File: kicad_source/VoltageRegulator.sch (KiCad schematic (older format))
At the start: 45 parts, among them CN6 691313710002, Q1 IPD90P03P4L- 04, U3 LM1085ISX-ADJ/NOPB, U9 IFX91041EJV

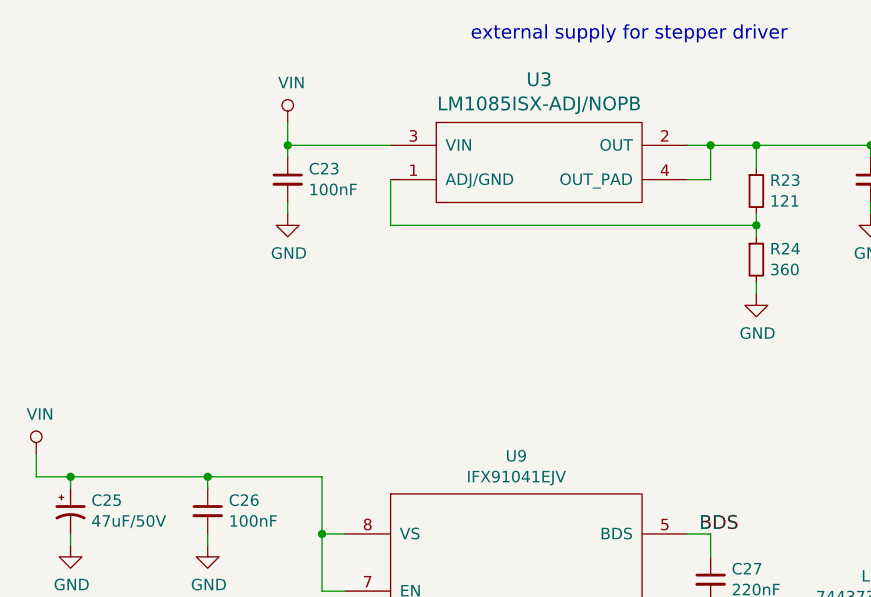
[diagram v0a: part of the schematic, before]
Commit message: corrected position of mounting holes for heat spreader, added information on input voltage
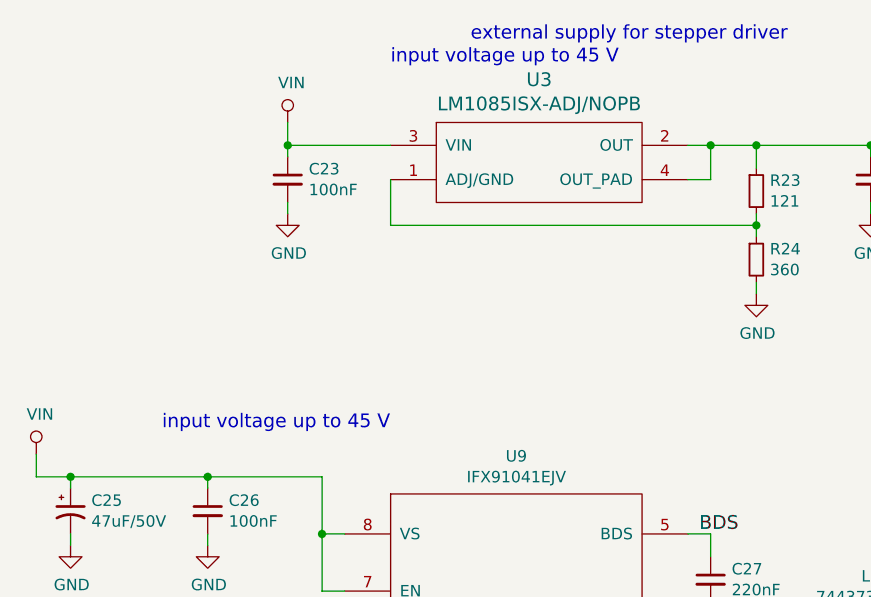
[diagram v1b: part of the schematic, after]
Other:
- note added: "input voltage up to 45 V"
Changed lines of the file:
@@
 Text Notes 4950 1200 0    60   ~ 0
 external supply for stepper driver
+Text Notes 3600 2900 0    60   ~ 0
+input voltage up to 45 V
+Text Notes 4600 1300 0    60   ~ 0
+input voltage up to 45 V
 $EndSCHEMATC

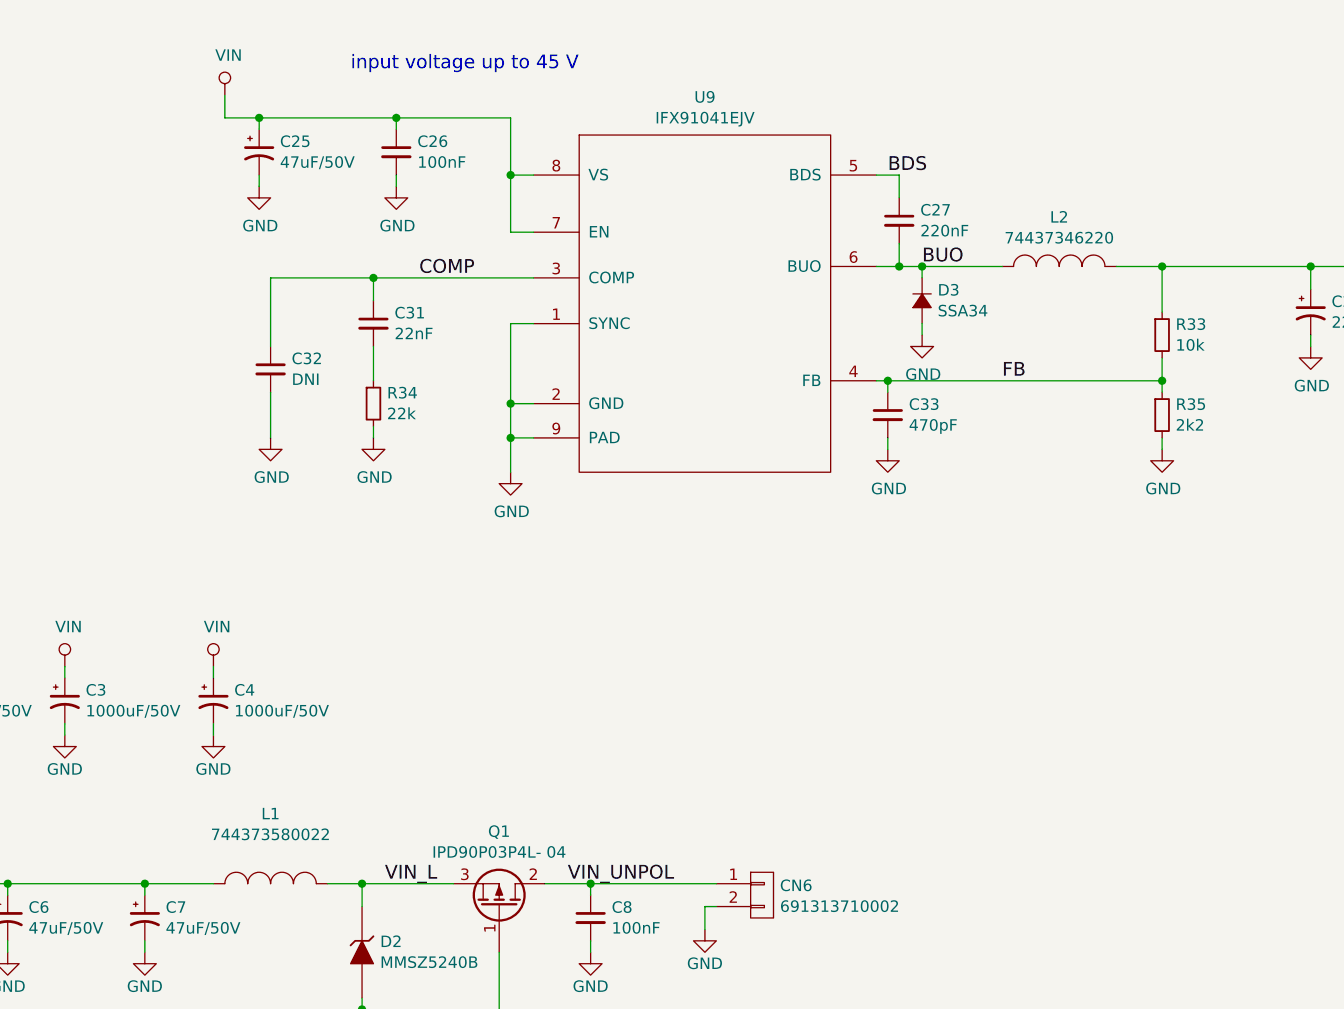
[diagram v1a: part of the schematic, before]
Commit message: changed L1 and L2 to Sumida 0624CDMCCDS for better availability
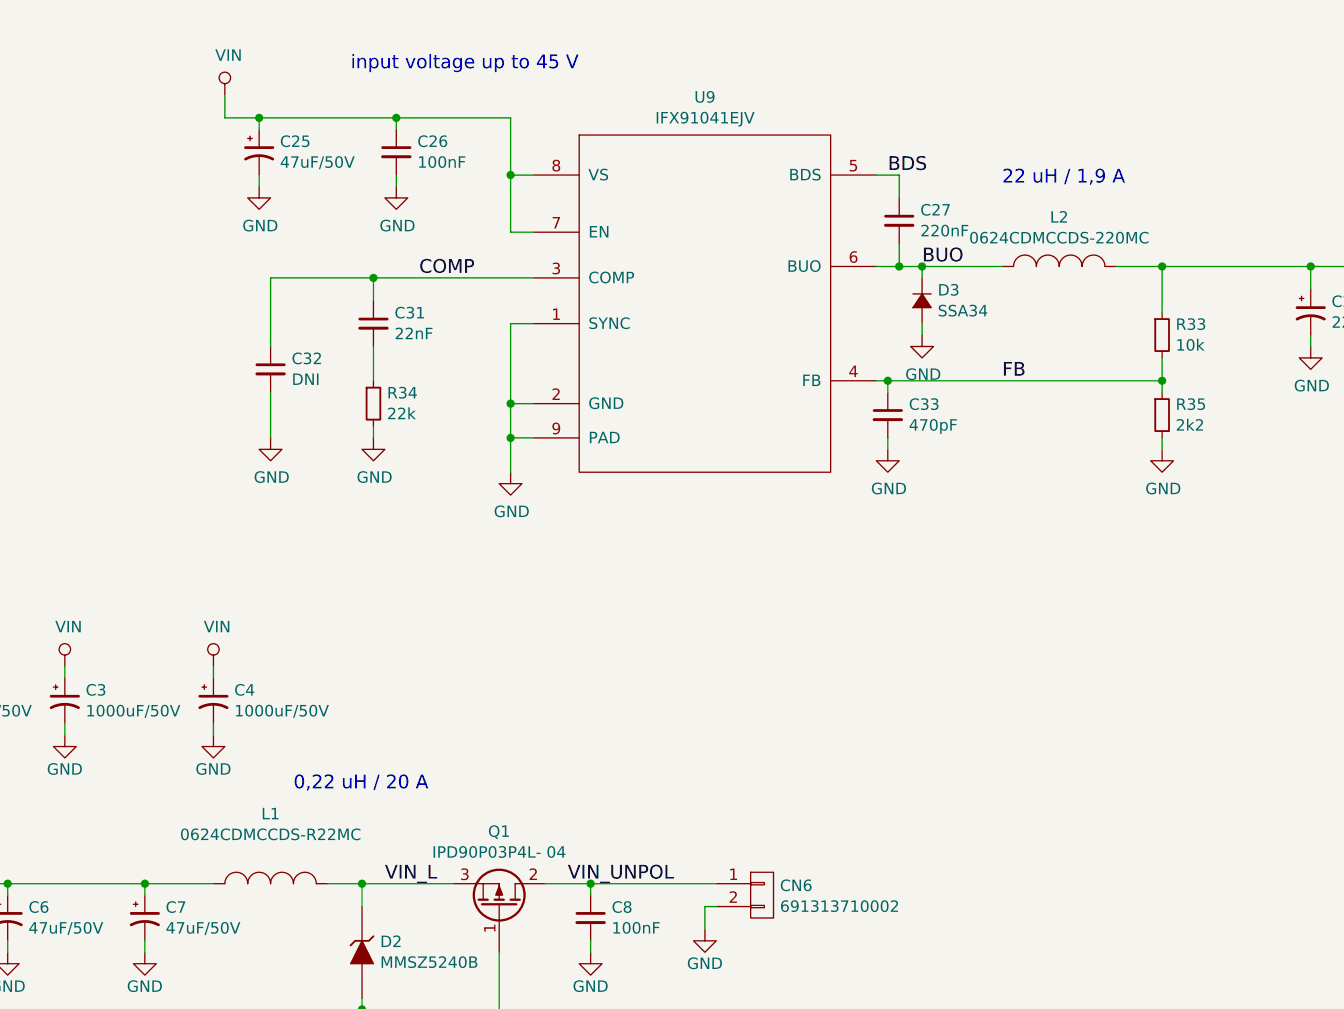
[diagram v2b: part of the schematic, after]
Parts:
- L1: value 744373580022 -> 0624CDMCCDS-R22MC; footprint L_power:WE-LHMI80xx -> L_power:Sumida-0624CDMCCDS
- L2: value 74437346220 -> 0624CDMCCDS-220MC; footprint L_power:WE-LHMI70xx -> L_power:Sumida-0624CDMCCDS
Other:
- note added: "0,22 uH / 20 A"
- note added: "22 uH / 1,9 A"
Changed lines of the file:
@@
 P 6700 3750
 F 0 "L2" H 6700 3965 50  0000 C CNN
-F 1 "74437346220" H 6700 3874 50  0000 C CNN
-F 2 "L_power:WE-LHMI70xx" H 6700 3873 50  0001 C CNN
+F 1 "0624CDMCCDS-220MC" H 6700 3874 50  0000 C CNN
+F 2 "L_power:Sumida-0624CDMCCDS" H 6700 3873 50  0001 C CNN
 F 3 "" H 6700 3750 50  0000 C CNN
 	1    6700 3750
@@
 AR Path="/5DE38154/5DEE0BBA" Ref="L1"  Part="1"
 F 0 "L1" H 3250 6755 50  0000 C CNN
-F 1 "744373580022" H 3250 6664 50  0000 C CNN
-F 2 "L_power:WE-LHMI80xx" H 3250 6573 50  0001 C CNN
+F 1 "0624CDMCCDS-R22MC" H 3250 6664 50  0000 C CNN
+F 2 "L_power:Sumida-0624CDMCCDS" H 3250 6573 50  0001 C CNN
 F 3 "" H 3250 6450 50  0000 C CNN
 	1    3250 6450
@@
 Text Notes 4600 1300 0    60   ~ 0
 input voltage up to 45 V
+Text Notes 3350 6050 0    60   ~ 0
+0,22 uH / 20 A
+Text Notes 6450 3400 0    60   ~ 0
+22 uH / 1,9 A
 $EndSCHEMATC

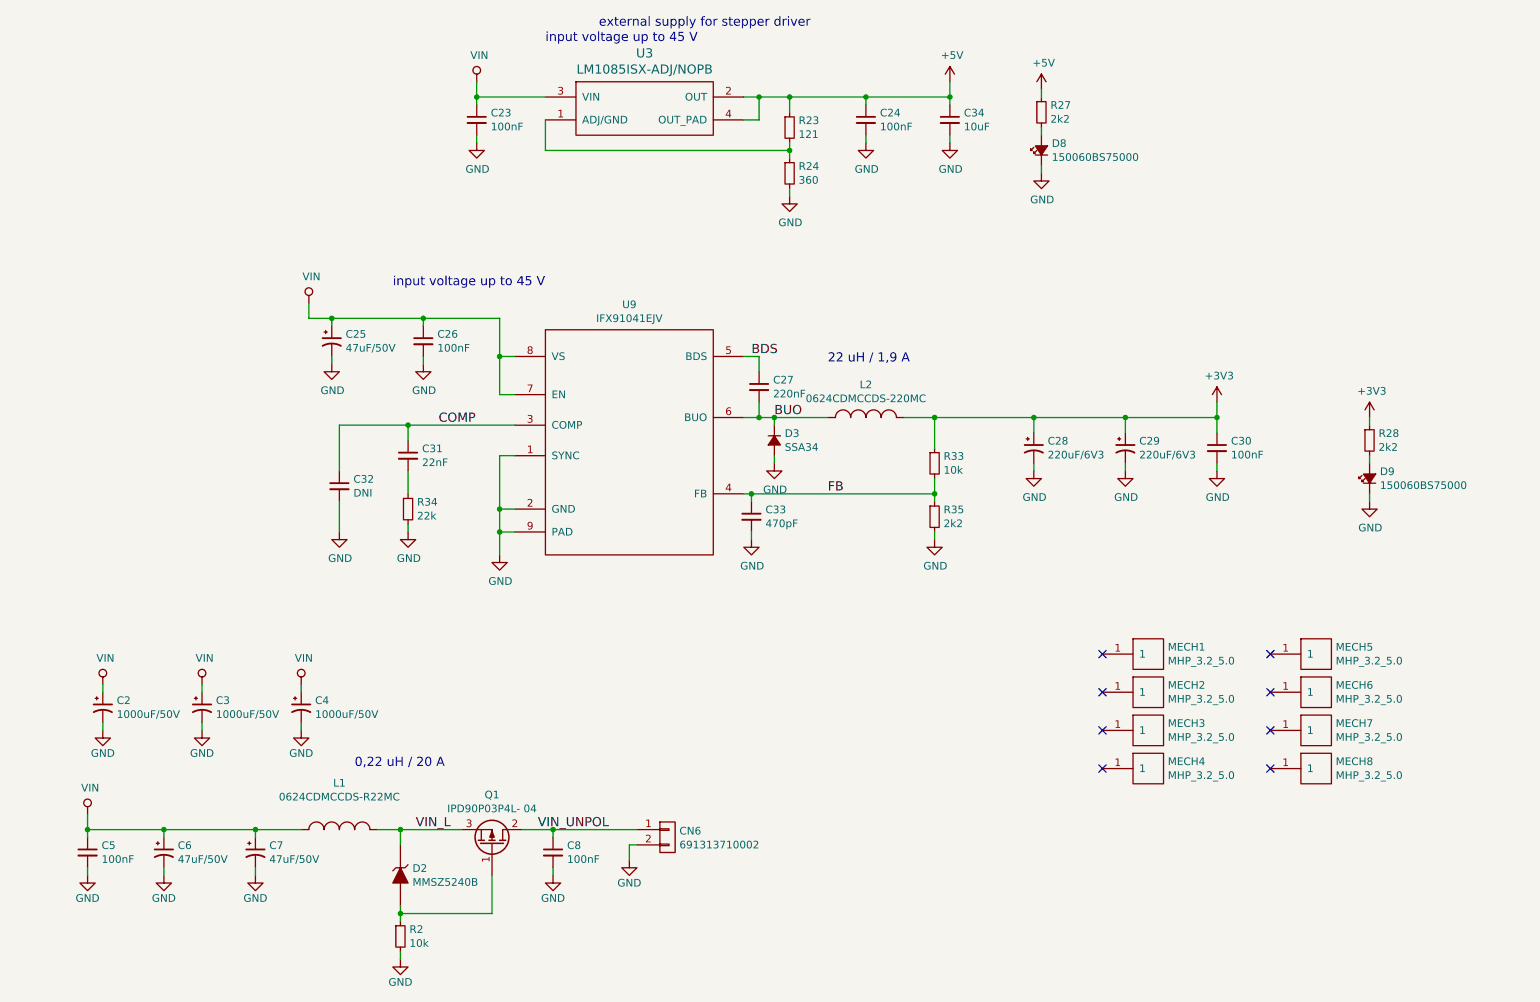
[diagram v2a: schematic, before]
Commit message: corrected order numbers of capacitors
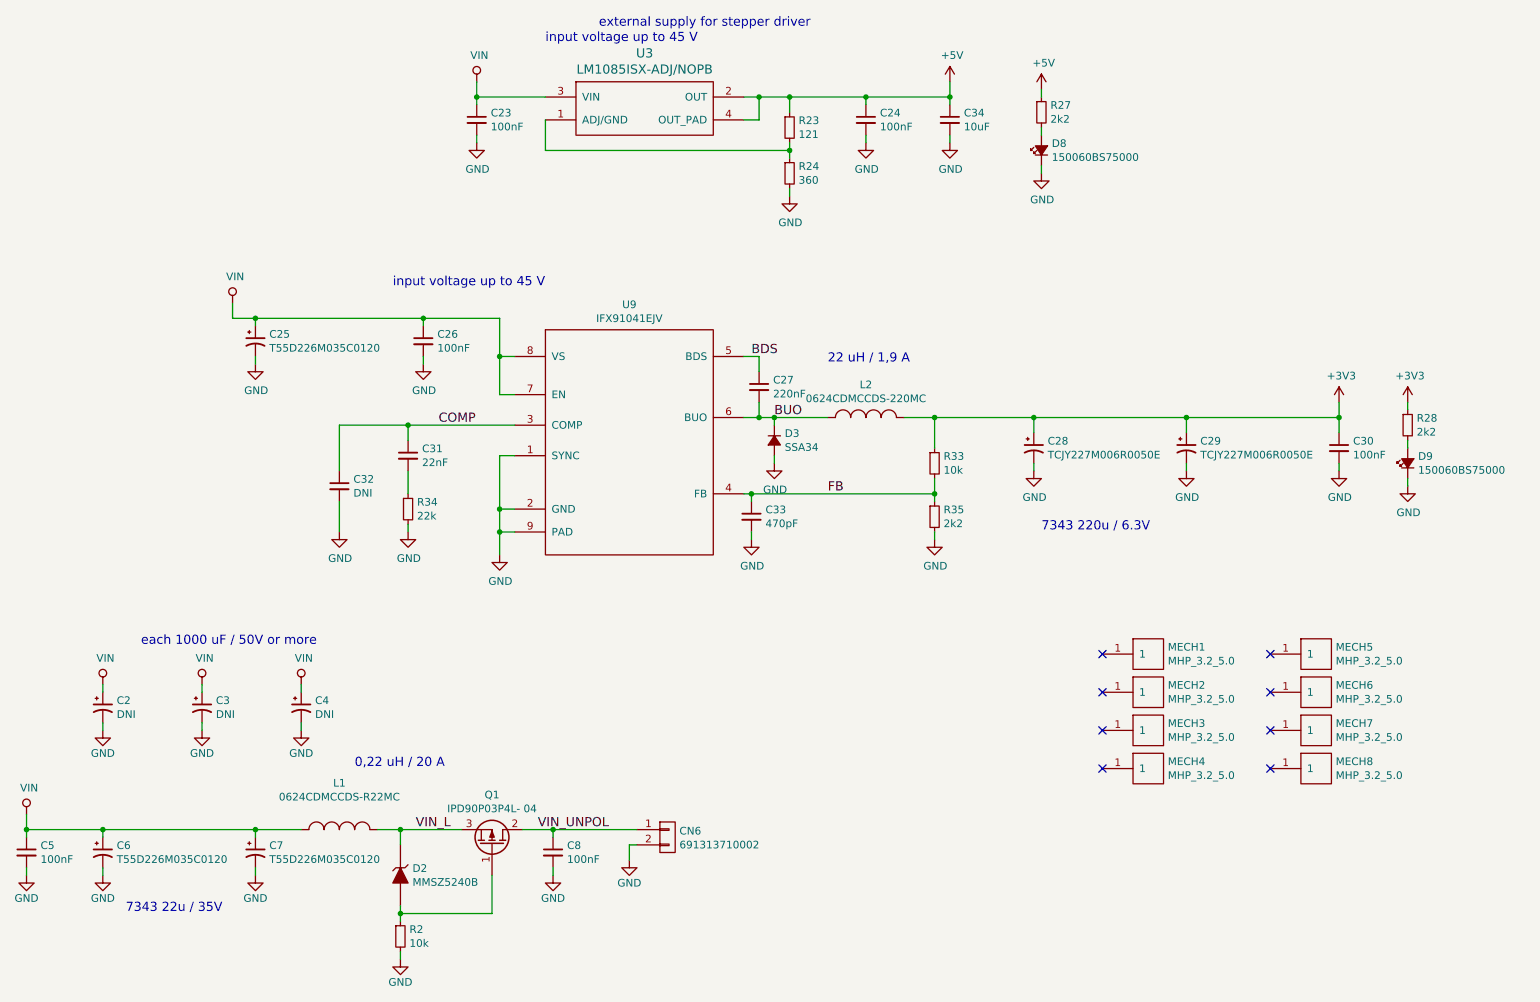
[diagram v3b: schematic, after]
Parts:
- C2, C3, C4: value 1000uF/50V -> DNI
- C25, C6, C7: value 47uF/50V -> T55D226M035C0120
- C28, C29: value 220uF/6V3 -> TCJY227M006R0050E
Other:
- note added: "7343 220u / 6.3V"
- note added: "7343 22u / 35V"
- note added: "each 1000 uF / 50V or more"
- moved on the sheet: C25, C29, C30, C5, C6, D9, R28
